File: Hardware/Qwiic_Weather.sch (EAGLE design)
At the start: 27 parts, among them J1 QWIIC, J2 QWIIC, J3 PTH, U1 BME280

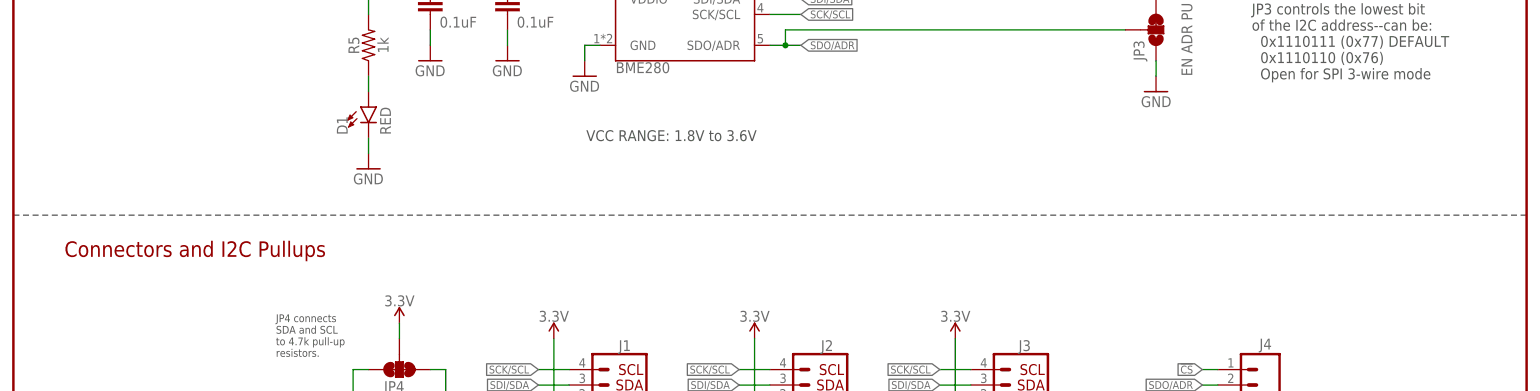
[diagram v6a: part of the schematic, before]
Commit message: Post double-check changes
-added IO warning in schematic
-removed leftover CCS811 text object in tNames
-designer name to vector
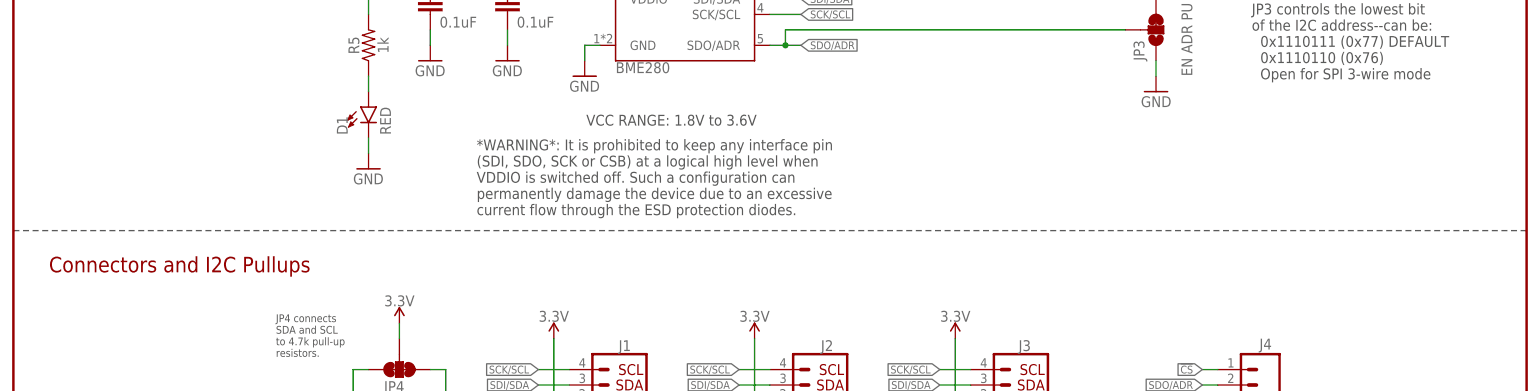
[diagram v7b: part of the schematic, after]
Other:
- note added: "*WARNING*: It is prohibited to keep any interface pin (SDI, SDO, SCK or CSB) at a logical high level when VDDIO is switched off. Such a configuration can permanently damage the device due to an excessive current flow through the ESD protection diodes."
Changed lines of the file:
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@@
 <grid distance="0.1" unitdist="inch" unit="inch" style="lines" multiple="1" display="no" altdistance="0.01" altunitdist="inch" altunit="inch"/>
 <layers>
-<layer number="1" name="Top" color="4" fill="1" visible="yes" active="no"/>
-<layer number="2" name="Route2" color="1" fill="3" visible="yes" active="no"/>
-<layer number="3" name="Route3" color="4" fill="3" visible="yes" active="no"/>
-<layer number="4" name="Route4" color="1" fill="4" visible="yes" active="no"/>
-<layer number="5" name="Route5" color="4" fill="4" visible="yes" active="no"/>
-<layer number="6" name="Route6" color="1" fill="8" visible="yes" active="no"/>
-<layer number="7" name="Route7" color="4" fill="8" visible="yes" active="no"/>
-<layer number="8" name="Route8" color="1" fill="2" visible="yes" active="no"/>
-<layer number="9" name="Route9" color="4" fill="2" visible="yes" active="no"/>
-<layer number="10" name="Route10" color="1" fill="7" visible="yes" active="no"/>
-<layer number="11" name="Route11" color="4" fill="7" visible="yes" active="no"/>
-<layer number="12" name="Route12" color="1" fill="5" visible="yes" active="no"/>
-<layer number="13" name="Route13" color="4" fill="5" visible="yes" active="no"/>
-<layer number="14" name="Route14" color="1" fill="6" visible="yes" active="no"/>
-<layer number="15" name="Route15" color="4" fill="6" visible="yes" active="no"/>
-<layer number="16" name="Bottom" color="1" fill="1" visible="yes" active="no"/>
-<layer number="17" name="Pads" color="2" fill="1" visible="yes" active="no"/>
-<layer number="18" name="Vias" color="2" fill="1" visible="yes" active="no"/>
-<layer number="19" name="Unrouted" color="6" fill="1" visible="yes" active="no"/>
-<layer number="20" name="Dimension" color="24" fill="1" visible="yes" active="no"/>
-<layer number="21" name="tPlace" color="16" fill="1" visible="yes" active="no"/>
-<layer number="22" name="bPlace" color="14" fill="1" visible="yes" active="no"/>
-<layer number="23" name="tOrigins" color="15" fill="1" visible="yes" active="no"/>
-<layer number="24" name="bOrigins" color="15" fill="1" visible="yes" active="no"/>
-<layer number="25" name="tNames" color="7" fill="1" visible="yes" active="no"/>
-<layer number="26" name="bNames" color="7" fill="1" visible="yes" active="no"/>
-<layer number="27" name="tValues" color="7" fill="1" visible="yes" active="no"/>
-<layer number="28" name="bValues" color="7" fill="1" visible="yes" active="no"/>
+<layer number="1" name="Top" color="4" fill="1" visible="no" active="no"/>
+<layer number="2" name="Route2" color="1" fill="3" visible="no" active="no"/>
+<layer number="3" name="Route3" color="4" fill="3" visible="no" active="no"/>
+<layer number="4" name="Route4" color="1" fill="4" visible="no" active="no"/>
+<layer number="5" name="Route5" color="4" fill="4" visible="no" active="no"/>
+<layer number="6" name="Route6" color="1" fill="8" visible="no" active="no"/>
+<layer number="7" name="Route7" color="4" fill="8" visible="no" active="no"/>
+<layer number="8" name="Route8" color="1" fill="2" visible="no" active="no"/>
+<layer number="9" name="Route9" color="4" fill="2" visible="no" active="no"/>
+<layer number="10" name="Route10" color="1" fill="7" visible="no" active="no"/>
+<layer number="11" name="Route11" color="4" fill="7" visible="no" active="no"/>
+<layer number="12" name="Route12" color="1" fill="5" visible="no" active="no"/>
+<layer number="13" name="Route13" color="4" fill="5" visible="no" active="no"/>
+<layer number="14" name="Route14" color="1" fill="6" visible="no" active="no"/>
+<layer number="15" name="Route15" color="4" fill="6" visible="no" active="no"/>
+<layer number="16" name="Bottom" color="1" fill="1" visible="no" active="no"/>
+<layer number="17" name="Pads" color="2" fill="1" visible="no" active="no"/>
+<layer number="18" name="Vias" color="2" fill="1" visible="no" active="no"/>
+<layer number="19" name="Unrouted" color="6" fill="1" visible="no" active="no"/>
+<layer number="20" name="Dimension" color="24" fill="1" visible="no" active="no"/>
+<layer number="21" name="tPlace" color="16" fill="1" visible="no" active="no"/>
+<layer number="22" name="bPlace" color="14" fill="1" visible="no" active="no"/>
+<layer number="23" name="tOrigins" color="15" fill="1" visible="no" active="no"/>
+<layer number="24" name="bOrigins" color="15" fill="1" visible="no" active="no"/>
+<layer number="25" name="tNames" color="7" fill="1" visible="no" active="no"/>
+<layer number="26" name="bNames" color="7" fill="1" visible="no" active="no"/>
+<layer number="27" name="tValues" color="7" fill="1" visible="no" active="no"/>
+<layer number="28" name="bValues" color="7" fill="1" visible="no" active="no"/>
 <layer number="29" name="tStop" color="7" fill="3" visible="no" active="no"/>
 <layer number="30" name="bStop" color="7" fill="6" visible="no" active="no"/>
@@
 <layer number="35" name="tGlue" color="7" fill="4" visible="no" active="no"/>
 <layer number="36" name="bGlue" color="7" fill="5" visible="no" active="no"/>
-<layer number="37" name="tTest" color="7" fill="1" visible="yes" active="no"/>
-<layer number="38" name="bTest" color="7" fill="1" visible="yes" active="no"/>
+<layer number="37" name="tTest" color="7" fill="1" visible="no" active="no"/>
+<layer number="38" name="bTest" color="7" fill="1" visible="no" active="no"/>
 <layer number="39" name="tKeepout" color="4" fill="11" visible="no" active="no"/>
 <layer number="40" name="bKeepout" color="1" fill="11" visible="no" active="no"/>
@@
 <layer number="44" name="Drills" color="7" fill="1" visible="no" active="no"/>
 <layer number="45" name="Holes" color="7" fill="1" visible="no" active="no"/>
-<layer number="46" name="Milling" color="3" fill="1" visible="yes" active="no"/>
-<layer number="47" name="Measures" color="7" fill="1" visible="yes" active="no"/>
-<layer number="48" name="Document" color="7" fill="1" visible="yes" active="no"/>
-<layer number="49" name="Reference" color="7" fill="1" visible="yes" active="no"/>
-<layer number="50" name="dxf" color="7" fill="1" visible="yes" active="no"/>
-<layer number="51" name="tDocu" color="6" fill="1" visible="yes" active="no"/>
-<layer number="52" name="bDocu" color="7" fill="1" visible="yes" active="no"/>
-<layer number="53" name="tGND_GNDA" color="7" fill="9" visible="yes" active="no"/>
-<layer number="54" name="bGND_GNDA" color="1" fill="9" visible="yes" active="no"/>
-<layer number="56" name="wert" color="7" fill="1" visible="yes" active="no"/>
-<layer number="57" name="tCAD" color="7" fill="1" visible="yes" active="no"/>
-<layer number="59" name="tCarbon" color="7" fill="1" visible="yes" active="no"/>
-<layer number="60" name="bCarbon" color="7" fill="1" visible="yes" active="no"/>
+<layer number="46" name="Milling" color="3" fill="1" visible="no" active="no"/>
+<layer number="47" name="Measures" color="7" fill="1" visible="no" active="no"/>
+<layer number="48" name="Document" color="7" fill="1" visible="no" active="no"/>
+<layer number="49" name="Reference" color="7" fill="1" visible="no" active="no"/>
+<layer number="50" name="dxf" color="7" fill="1" visible="no" active="no"/>
+<layer number="51" name="tDocu" color="6" fill="1" visible="no" active="no"/>
+<layer number="52" name="bDocu" color="7" fill="1" visible="no" active="no"/>
+<layer number="53" name="tGND_GNDA" color="7" fill="9" visible="no" active="no"/>
+<layer number="54" name="bGND_GNDA" color="1" fill="9" visible="no" active="no"/>
+<layer number="56" name="wert" color="7" fill="1" visible="no" active="no"/>
+<layer number="57" name="tCAD" color="7" fill="1" visible="no" active="no"/>
+<layer number="59" name="tCarbon" color="7" fill="1" visible="no" active="no"/>
+<layer number="60" name="bCarbon" color="7" fill="1" visible="no" active="no"/>
 <layer number="88" name="SimResults" color="9" fill="1" visible="no" active="yes"/>
 <layer number="89" name="SimProbes" color="9" fill="1" visible="no" active="yes"/>
@@
 <text x="238.76" y="7.62" size="2.54" layer="94" font="vector" align="center-left">v10</text>
 <text x="165.862" y="11.176" size="2.54" layer="94" font="vector">Kenny Hora, Pete Lewis</text>
-<wire x1="248.92" y1="83.82" x2="0" y2="83.82" width="0.2032" layer="97" style="shortdash"/>
+<wire x1="248.92" y1="81.28" x2="0" y2="81.28" width="0.2032" layer="97" style="shortdash"/>
 <text x="135.636" y="145.288" size="1.778" layer="97" font="vector" align="top-left">DEFAULT: I2C mode</text>
 <text x="5.842" y="178.562" size="2.54" layer="94" font="vector" rot="MR180" align="top-left">BME280 - Humidty, Pressure, Temperature </text>
@@
   SPI 3-WIRE:
     SJ3 must be opened.</text>
-<text x="94.234" y="96.012" size="1.778" layer="97" font="vector">VCC RANGE: 1.8V to 3.6V</text>
-<text x="8.382" y="76.962" size="2.54" layer="94" font="vector" rot="MR180" align="top-left">Connectors and I2C Pullups</text>
+<text x="94.234" y="98.552" size="1.778" layer="97" font="vector">VCC RANGE: 1.8V to 3.6V</text>
+<text x="5.842" y="74.422" size="2.54" layer="94" font="vector" rot="MR180" align="top-left">Connectors and I2C Pullups</text>
 <text x="52.324" y="126.492" size="1.778" layer="97" font="vector" align="top-right">Cut JP1 to
 disable power LED</text>
+<text x="76.2" y="83.82" size="1.778" layer="97" font="vector">*WARNING*: It is prohibited to keep any interface pin
+(SDI, SDO, SCK or CSB) at a logical high level when
+VDDIO is switched off. Such a configuration can
+permanently damage the device due to an excessive
+current flow through the ESD protection diodes.</text>
 </plain>
 <instances>
